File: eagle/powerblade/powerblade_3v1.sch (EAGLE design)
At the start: 93 parts, among them J1 JTAG_14PIN_IDC, J21 AC_INTBFILM, J4 TC2030-JLINK-NL, Q1 2N7002, Q3 2SK1829, Q4 2SK1829, U1 TPS62122, U2 MCP6V3, U3 MSP430FR5738, U4 NRF51822QF, U6 MAX9910, U7 OPA2369, X1 16MHz, X2 ABS05-32.768KHZ-9-T, X3 32.768kHz

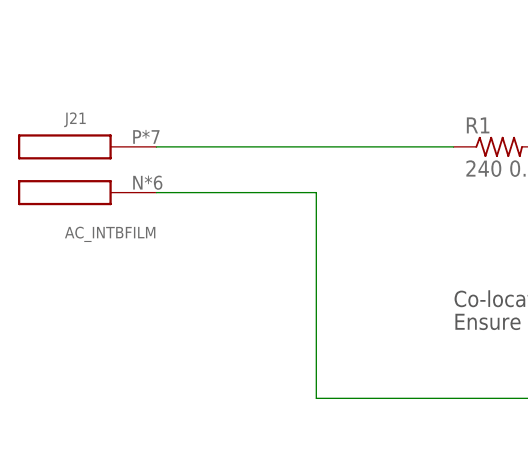
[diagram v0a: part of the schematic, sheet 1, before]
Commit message: updated phase and neutral and updated in powerblade
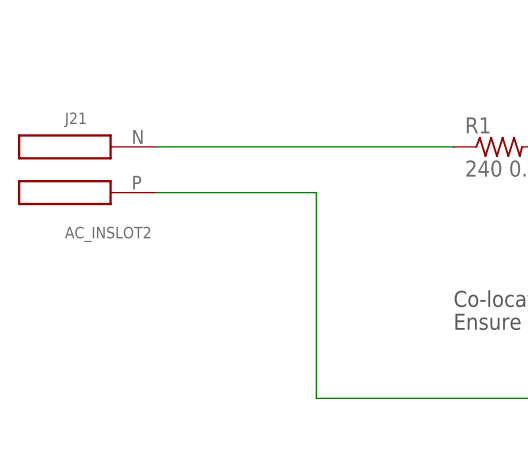
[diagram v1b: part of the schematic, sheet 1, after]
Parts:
- J21: value AC_INTBFILM -> AC_INSLOT2; device powerfilm:AC_INTBFILM -> powerfilm:AC_INSLOT2
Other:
- moved on the sheet: J21
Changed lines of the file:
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@@
 <part name="GND1" library="supply1" deviceset="GND" device=""/>
 <part name="P+1" library="supply1" deviceset="VCC" device=""/>
-<part name="J21" library="powerfilm" deviceset="AC_IN" device="TBFILM" value="AC_INTBFILM">
+<part name="J21" library="powerfilm" deviceset="AC_IN" device="SLOT2" value="AC_INSLOT2">
 <attribute name="DIGIKEY" value="NP"/>
 </part>

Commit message: updates to powerblade board
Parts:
- removed C1: 0.033uF 250VAC, rcl:C-EUC2220K
- removed R1: 240 0.25W, rcl:R-US_R0603
- removed R8: 1M, rcl:R-US_R0603
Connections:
- removed net N$12: J21.P, R1.1
- net N$2: no longer C1.1, R8.2
- net VTEST: now also J21.P; no longer C1.2, R1.2, R8.1
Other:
- moved on the sheet: R3

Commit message: placement work for powerblade 3v1
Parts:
- added C1: 33uF, rcl:CPOL-US0805_SM
- C10, C3, C7: device rcl:C-EUC0603 -> rcl:C-EUC0603_SM
- C28, C4, C8, C9: device rcl:C-EUC0402 -> rcl:C-EUC0402_SM
- C5: device rcl:C-EUC0603 -> rcl:C-EUC0805_SM
- R20, R21, R7, R9, RF, RI1, RI2: device rcl:R-US_R0402 -> rcl:R-US_R0402_SM
- R24: device rcl:R-US_R0603 -> rcl:R-US_R0603_SM
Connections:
- net +3V3: now also C5.1
- net GND: now also C1.-
- net VCC: now also C1.+; no longer C5.1

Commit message: changed v_sense amplifier to TI part
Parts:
- U6: DIGIKEY (none) -> 296-25252-1-ND
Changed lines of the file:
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@@
 <?xml version="1.0" encoding="utf-8"?>
 <!DOCTYPE eagle SYSTEM "eagle.dtd">
-<eagle version="6.3">
+<eagle version="6.5.0">
 <drawing>
 <settings>
@@
 <grid distance="0.1" unitdist="inch" unit="inch" style="lines" multiple="1" display="no" altdistance="0.01" altunitdist="inch" altunit="inch"/>
 <layers>
-<layer number="1" name="Top" color="4" fill="1" visible="yes" active="no"/>
-<layer number="2" name="Route2" color="1" fill="3" visible="yes" active="no"/>
-<layer number="3" name="Route3" color="4" fill="3" visible="yes" active="no"/>
-<layer number="4" name="Route4" color="1" fill="4" visible="yes" active="no"/>
-<layer number="5" name="Route5" color="4" fill="4" visible="yes" active="no"/>
-<layer number="6" name="Route6" color="1" fill="8" visible="yes" active="no"/>
-<layer number="7" name="Route7" color="4" fill="8" visible="yes" active="no"/>
-<layer number="8" name="Route8" color="1" fill="2" visible="yes" active="no"/>
-<layer number="9" name="Route9" color="4" fill="2" visible="yes" active="no"/>
-<layer number="10" name="Route10" color="1" fill="7" visible="yes" active="no"/>
-<layer number="11" name="Route11" color="4" fill="7" visible="yes" active="no"/>
-<layer number="12" name="Route12" color="1" fill="5" visible="yes" active="no"/>
-<layer number="13" name="Route13" color="4" fill="5" visible="yes" active="no"/>
-<layer number="14" name="Route14" color="1" fill="6" visible="yes" active="no"/>
-<layer number="15" name="Route15" color="4" fill="6" visible="yes" active="no"/>
-<layer number="16" name="Bottom" color="1" fill="1" visible="yes" active="no"/>
-<layer number="17" name="Pads" color="2" fill="1" visible="yes" active="no"/>
-<layer number="18" name="Vias" color="2" fill="1" visible="yes" active="no"/>
-<layer number="19" name="Unrouted" color="6" fill="1" visible="yes" active="no"/>
-<layer number="20" name="Dimension" color="15" fill="1" visible="yes" active="no"/>
-<layer number="21" name="tPlace" color="7" fill="1" visible="yes" active="no"/>
-<layer number="22" name="bPlace" color="7" fill="1" visible="yes" active="no"/>
-<layer number="23" name="tOrigins" color="15" fill="1" visible="yes" active="no"/>
-<layer number="24" name="bOrigins" color="15" fill="1" visible="yes" active="no"/>
-<layer number="25" name="tNames" color="7" fill="1" visible="yes" active="no"/>
-<layer number="26" name="bNames" color="7" fill="1" visible="yes" active="no"/>
-<layer number="27" name="tValues" color="7" fill="1" visible="yes" active="no"/>
-<layer number="28" name="bValues" color="7" fill="1" visible="yes" active="no"/>
+<layer number="1" name="Top" color="4" fill="1" visible="no" active="no"/>
+<layer number="2" name="Route2" color="1" fill="3" visible="no" active="no"/>
+<layer number="3" name="Route3" color="4" fill="3" visible="no" active="no"/>
+<layer number="4" name="Route4" color="1" fill="4" visible="no" active="no"/>
+<layer number="5" name="Route5" color="4" fill="4" visible="no" active="no"/>
+<layer number="6" name="Route6" color="1" fill="8" visible="no" active="no"/>
+<layer number="7" name="Route7" color="4" fill="8" visible="no" active="no"/>
+<layer number="8" name="Route8" color="1" fill="2" visible="no" active="no"/>
+<layer number="9" name="Route9" color="4" fill="2" visible="no" active="no"/>
+<layer number="10" name="Route10" color="1" fill="7" visible="no" active="no"/>
+<layer number="11" name="Route11" color="4" fill="7" visible="no" active="no"/>
+<layer number="12" name="Route12" color="1" fill="5" visible="no" active="no"/>
+<layer number="13" name="Route13" color="4" fill="5" visible="no" active="no"/>
+<layer number="14" name="Route14" color="1" fill="6" visible="no" active="no"/>
+<layer number="15" name="Route15" color="4" fill="6" visible="no" active="no"/>
+<layer number="16" name="Bottom" color="1" fill="1" visible="no" active="no"/>
+<layer number="17" name="Pads" color="2" fill="1" visible="no" active="no"/>
+<layer number="18" name="Vias" color="2" fill="1" visible="no" active="no"/>
+<layer number="19" name="Unrouted" color="6" fill="1" visible="no" active="no"/>
+<layer number="20" name="Dimension" color="15" fill="1" visible="no" active="no"/>
+<layer number="21" name="tPlace" color="7" fill="1" visible="no" active="no"/>
+<layer number="22" name="bPlace" color="7" fill="1" visible="no" active="no"/>
+<layer number="23" name="tOrigins" color="15" fill="1" visible="no" active="no"/>
+<layer number="24" name="bOrigins" color="15" fill="1" visible="no" active="no"/>
+<layer number="25" name="tNames" color="7" fill="1" visible="no" active="no"/>
+<layer number="26" name="bNames" color="7" fill="1" visible="no" active="no"/>
+<layer number="27" name="tValues" color="7" fill="1" visible="no" active="no"/>
+<layer number="28" name="bValues" color="7" fill="1" visible="no" active="no"/>
 <layer number="29" name="tStop" color="7" fill="3" visible="no" active="no"/>
 <layer number="30" name="bStop" color="7" fill="6" visible="no" active="no"/>
@@
 <layer number="35" name="tGlue" color="7" fill="4" visible="no" active="no"/>
 <layer number="36" name="bGlue" color="7" fill="5" visible="no" active="no"/>
-<layer number="37" name="tTest" color="7" fill="1" visible="yes" active="no"/>
-<layer number="38" name="bTest" color="7" fill="1" visible="yes" active="no"/>
+<layer number="37" name="tTest" color="7" fill="1" visible="no" active="no"/>
+<layer number="38" name="bTest" color="7" fill="1" visible="no" active="no"/>
 <layer number="39" name="tKeepout" color="4" fill="11" visible="no" active="no"/>
 <layer number="40" name="bKeepout" color="1" fill="11" visible="no" active="no"/>
@@
 <layer number="44" name="Drills" color="7" fill="1" visible="no" active="no"/>
 <layer number="45" name="Holes" color="7" fill="1" visible="no" active="no"/>
-<layer number="46" name="Milling" color="3" fill="1" visible="yes" active="no"/>
-<layer number="47" name="Measures" color="7" fill="1" visible="yes" active="no"/>
-<layer number="48" name="Document" color="7" fill="1" visible="yes" active="no"/>
-<layer number="49" name="Reference" color="7" fill="1" visible="yes" active="no"/>
-<layer number="50" name="dxf" color="7" fill="1" visible="yes" active="no"/>
-<layer number="51" name="tDocu" color="7" fill="1" visible="yes" active="no"/>
-<layer number="52" name="bDocu" color="7" fill="1" visible="yes" active="no"/>
-<layer number="53" name="tGND_GNDA" color="7" fill="9" visible="yes" active="no"/>
-<layer number="54" name="bGND_GNDA" color="1" fill="9" visible="yes" active="no"/>
-<layer number="56" name="wert" color="7" fill="1" visible="yes" active="no"/>
-<layer number="57" name="tCAD" color="7" fill="1" visible="yes" active="no"/>
+<layer number="46" name="Milling" color="3" fill="1" visible="no" active="no"/>
+<layer number="47" name="Measures" color="7" fill="1" visible="no" active="no"/>
+<layer number="48" name="Document" color="7" fill="1" visible="no" active="no"/>
+<layer number="49" name="Reference" color="7" fill="1" visible="no" active="no"/>
+<layer number="50" name="dxf" color="7" fill="1" visible="no" active="no"/>
+<layer number="51" name="tDocu" color="7" fill="1" visible="no" active="no"/>
+<layer number="52" name="bDocu" color="7" fill="1" visible="no" active="no"/>
+<layer number="53" name="tGND_GNDA" color="7" fill="9" visible="no" active="no"/>
+<layer number="54" name="bGND_GNDA" color="1" fill="9" visible="no" active="no"/>
+<layer number="56" name="wert" color="7" fill="1" visible="no" active="no"/>
+<layer number="57" name="tCAD" color="7" fill="1" visible="no" active="no"/>
 <layer number="91" name="Nets" color="2" fill="1" visible="yes" active="yes"/>
 <layer number="92" name="Busses" color="1" fill="1" visible="yes" active="yes"/>
@@
 <attribute name="DIGIKEY" value="445-1265-1-ND"/>
 </part>
-<part name="U6" library="powerfilm" deviceset="MAX9910" device=""/>
+<part name="U6" library="powerfilm" deviceset="MAX9910" device="">
+<attribute name="DIGIKEY" value="296-25252-1-ND"/>
+</part>
 <part name="C28" library="rcl" deviceset="C-EU" device="C0402_SM" value="0.1uF">
 <attribute name="DIGIKEY" value="445-1265-1-ND"/>

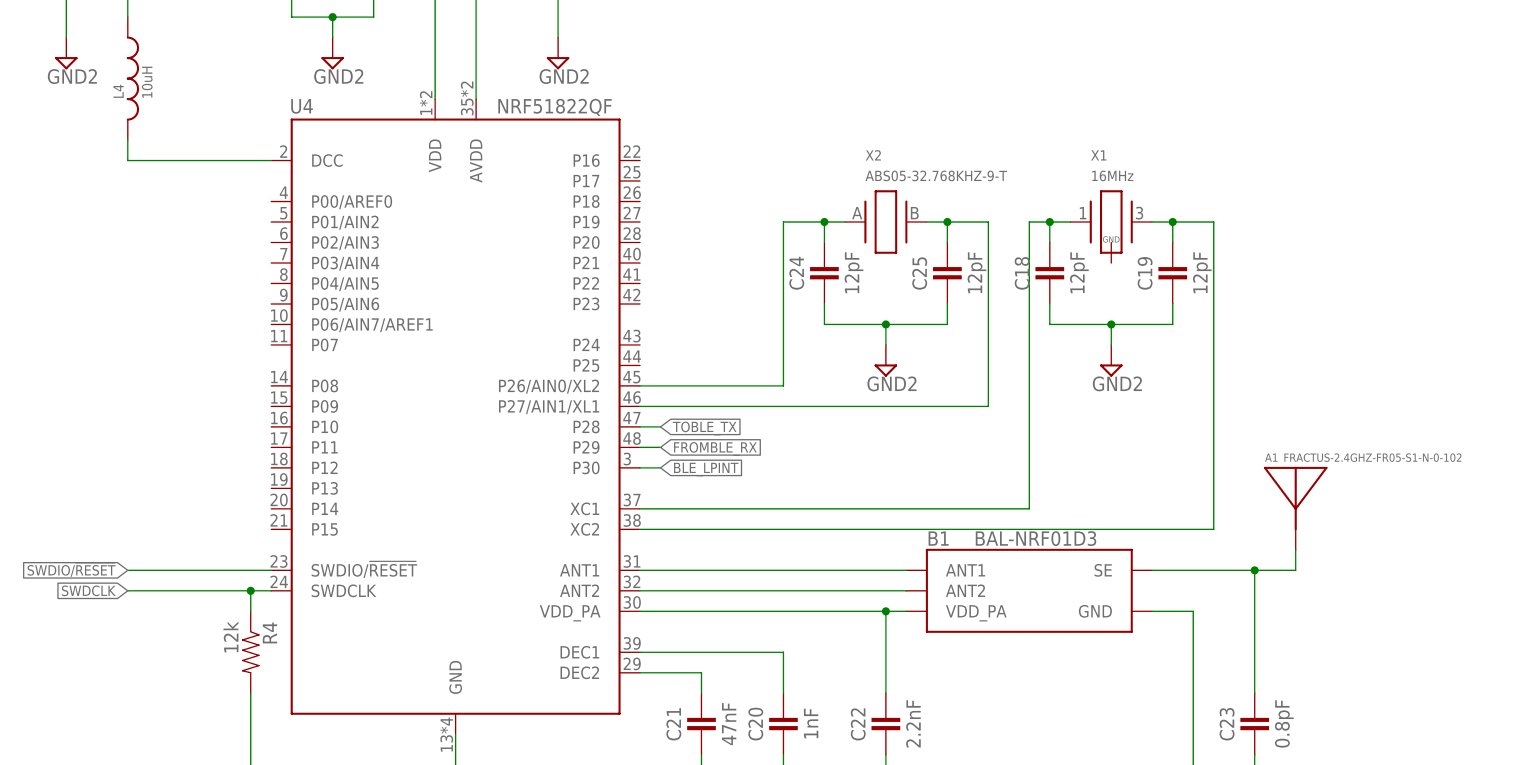
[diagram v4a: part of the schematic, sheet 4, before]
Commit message: placement for 51822 and 0402_sm for all passives in current sense
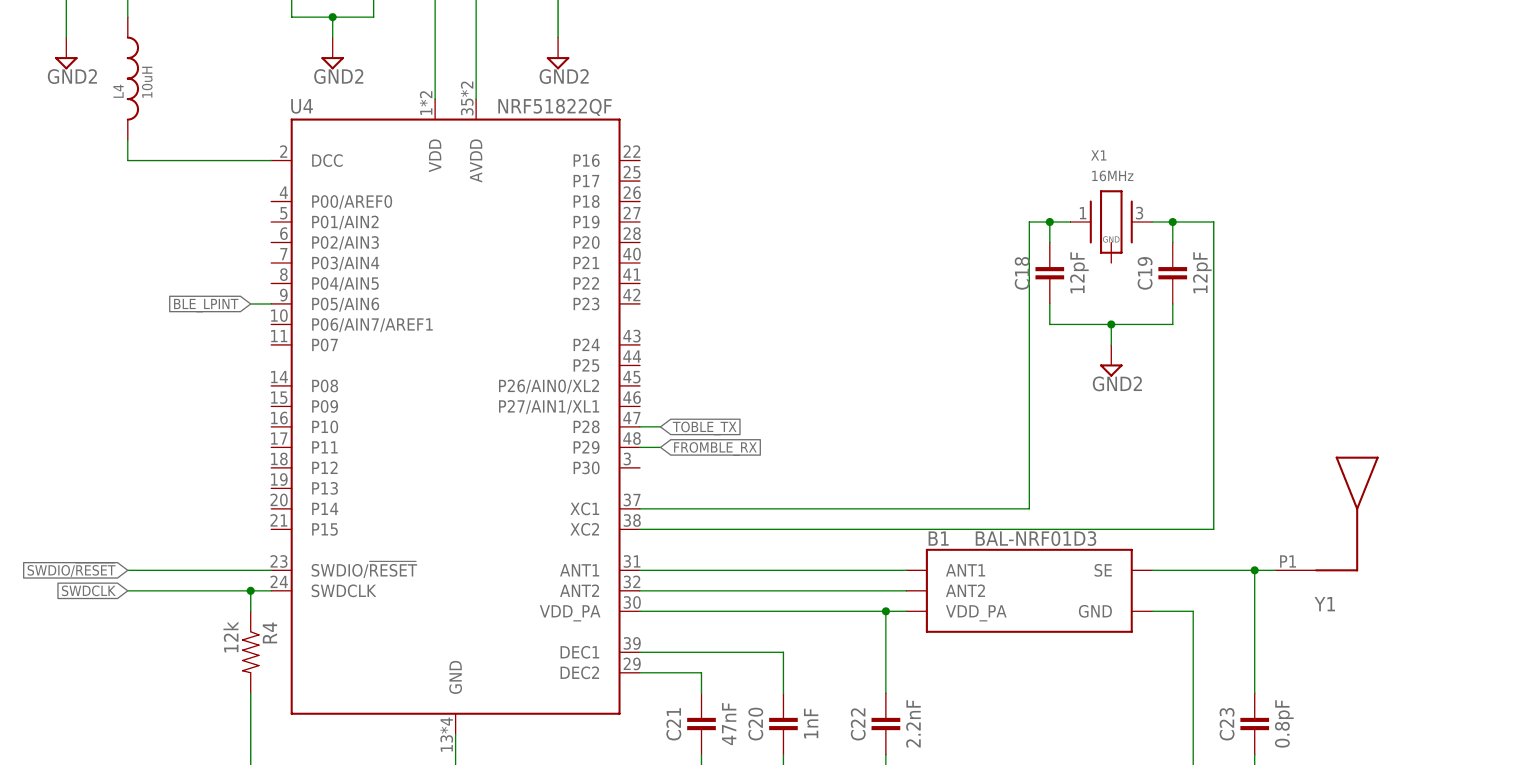
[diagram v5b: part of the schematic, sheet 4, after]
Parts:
- removed A1: FRACTUS-2.4GHZ-FR05-S1-N-0-102, chips:FRACTUS-2.4GHZ-FR05-S1-N-0-102
- removed C24, C25: 12pF, passives:CAPACITOR
- removed X2: ABS05-32.768KHZ-9-T, crystals:ABS05-32.768KHZ-9-T
- added R1: NP, rcl:R-US_R0402_SM
- added Y1: UREACH_XTEND, powerfilm:UREACH_XTEND
- C2: device rcl:C-EUC0603 -> rcl:C-EUC0402_SM
- C27, C38, C39: device rcl:C-EUC0402 -> rcl:C-EUC0402_SM
- R14, R15, R16, R17, R18, R35, R37, R38, R39, R40: device rcl:R-US_R0402 -> rcl:R-US_R0402_SM
- R2, R5: device rcl:R-US_R0603 -> rcl:R-US_R0402_SM
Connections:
- removed net A0: C24.1, U4.P26/AIN0/XL2, X2.1
- removed net A1: C25.1, U4.P27/AIN1/XL1, X2.2
- net BLE_LPINT: now also U4.P05/AIN6; no longer U4.P30
- net GND2: no longer C24.2, C25.2
- net N$37: now also R1.1
- net N$4: now also Y1.P1; no longer A1.ANTENNA
- net N$65: now also R1.2

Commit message: finished placement
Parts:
- C14: device rcl:C-EUC0603 -> rcl:C-EUC0402_SM; DIGIKEY 445-1316-1-ND -> (none)
- C15: device rcl:C-EUC0603 -> rcl:C-EUC0603_SM; DIGIKEY 1276-1119-1-ND -> (none)
- C16, C34, C6: device rcl:C-EUC0603 -> rcl:C-EUC0402_SM
- R10, R11, R12, R13, R22: device rcl:R-US_R0603 -> rcl:R-US_R0402_SM
- R19: device rcl:R-US_R0603 -> rcl:R-US_R0402_SM; DIGIKEY P47KGCT-ND -> (none)
- R6: device rcl:R-US_R0603 -> rcl:R-US_R0603_SM
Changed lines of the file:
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@@
 </part>
 <part name="U3" library="powerfilm" deviceset="MSP430FR5738" device=""/>
-<part name="C14" library="rcl" deviceset="C-EU" device="C0603" value="0.1uF">
-<attribute name="DIGIKEY" value="445-1316-1-ND"/>
-</part>
-<part name="C15" library="rcl" deviceset="C-EU" device="C0603" value="10uF">
-<attribute name="DIGIKEY" value="1276-1119-1-ND"/>
-</part>
-<part name="C16" library="rcl" deviceset="C-EU" device="C0603" value="470nF">
+<part name="C14" library="rcl" deviceset="C-EU" device="C0402_SM" value="0.1uF"/>
+<part name="C15" library="rcl" deviceset="C-EU" device="C0603_SM" value="10uF"/>
+<part name="C16" library="rcl" deviceset="C-EU" device="C0402_SM" value="470nF">
 <attribute name="DIGIKEY" value="445-5192-1-ND"/>
 </part>
@@
 <part name="GND21" library="supply1" deviceset="GND" device=""/>
 <part name="+3V4" library="supply1" deviceset="+3V3" device=""/>
-<part name="R19" library="rcl" deviceset="R-US_" device="R0603" value="47k">
-<attribute name="DIGIKEY" value="P47KGCT-ND"/>
-</part>
+<part name="R19" library="rcl" deviceset="R-US_" device="R0402_SM" value="47k"/>
 <part name="GND22" library="supply1" deviceset="GND" device=""/>
 <part name="J1" library="ibat" deviceset="JTAG_14PIN" device="_IDC" value="JTAG_14PIN_IDC">
@@
 <part name="+3V7" library="supply1" deviceset="+3V3" device=""/>
 <part name="GND23" library="supply1" deviceset="GND" device=""/>
-<part name="R11" library="rcl" deviceset="R-US_" device="R0603" value="670k"/>
-<part name="R12" library="rcl" deviceset="R-US_" device="R0603" value="330k"/>
+<part name="R11" library="rcl" deviceset="R-US_" device="R0402_SM" value="670k"/>
+<part name="R12" library="rcl" deviceset="R-US_" device="R0402_SM" value="330k"/>
 <part name="GND25" library="supply1" deviceset="GND" device=""/>
 <part name="P+4" library="supply1" deviceset="VCC" device=""/>
@@
 <attribute name="DIGIKEY" value="535-12373-1-ND"/>
 </part>
-<part name="C6" library="rcl" deviceset="C-EU" device="C0603" value="8pF">
+<part name="C6" library="rcl" deviceset="C-EU" device="C0402_SM" value="8pF">
 <attribute name="DIGIKEY" value="1276-1817-1-ND"/>
 </part>
-<part name="C34" library="rcl" deviceset="C-EU" device="C0603" value="8pF">
+<part name="C34" library="rcl" deviceset="C-EU" device="C0402_SM" value="8pF">
 <attribute name="DIGIKEY" value="1276-1817-1-ND"/>
 </part>
@@
 <part name="Q4" library="powerfilm" deviceset="2SK1829" device=""/>
 <part name="SUPPLY19" library="supply2" deviceset="GND3" device=""/>
-<part name="R6" library="rcl" deviceset="R-US_" device="R0603" value="660k"/>
+<part name="R6" library="rcl" deviceset="R-US_" device="R0603_SM" value="660k"/>
 <part name="SUPPLY20" library="supply2" deviceset="GND3" device=""/>
 <part name="SUPPLY21" library="supply2" deviceset="GND3" device=""/>
@@
 <part name="SUPPLY28" library="supply2" deviceset="GND3" device=""/>
 <part name="GND2" library="supply1" deviceset="GND" device=""/>
-<part name="R10" library="rcl" deviceset="R-US_" device="R0603" value="220k"/>
-<part name="R13" library="rcl" deviceset="R-US_" device="R0603" value="330k"/>
-<part name="R22" library="rcl" deviceset="R-US_" device="R0603" value="670k"/>
+<part name="R10" library="rcl" deviceset="R-US_" device="R0402_SM" value="220k"/>
+<part name="R13" library="rcl" deviceset="R-US_" device="R0402_SM" value="330k"/>
+<part name="R22" library="rcl" deviceset="R-US_" device="R0402_SM" value="670k"/>
 <part name="GND8" library="supply1" deviceset="GND" device=""/>
 <part name="R24" library="rcl" deviceset="R-US_" device="R0603_SM" value="1 1%">
@@
 <instances>
 <instance part="U3" gate="G$1" x="0" y="0"/>
-<instance part="C14" gate="G$1" x="-35.56" y="35.56">
-<attribute name="DIGIKEY" x="-35.56" y="35.56" size="1.27" layer="96" display="off"/>
-</instance>
-<instance part="C15" gate="G$1" x="-45.72" y="35.56">
-<attribute name="DIGIKEY" x="-45.72" y="35.56" size="1.27" layer="96" display="off"/>
-</instance>
+<instance part="C14" gate="G$1" x="-35.56" y="35.56"/>
+<instance part="C15" gate="G$1" x="-45.72" y="35.56"/>
 <instance part="C16" gate="G$1" x="-43.18" y="15.24" smashed="yes" rot="R90">
 <attribute name="NAME" x="-41.656" y="18.161" size="1.778" layer="95"/>
@@
 <instance part="GND21" gate="1" x="-48.26" y="10.16"/>
 <instance part="+3V4" gate="G$1" x="-35.56" y="50.8"/>
-<instance part="R19" gate="G$1" x="-55.88" y="33.02" rot="R90">
-<attribute name="DIGIKEY" x="-55.88" y="33.02" size="1.27" layer="96" rot="R90" display="off"/>
-</instance>
+<instance part="R19" gate="G$1" x="-55.88" y="33.02" rot="R90"/>
 <instance part="GND22" gate="1" x="27.94" y="-27.94"/>
 <instance part="J1" gate="G$1" x="17.78" y="48.26">

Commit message: updates and routing in powerblade
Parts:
- removed C13: 4.7uF, passives:CAPACITOR
- added C24: 0.1uF, rcl:C-EUC0402_SM
- added TP4, TP5, TP6, TP7, TP8: TP_LONG, skyspecs:TP_LONG
- C11: value 0.1uF -> 4.7uF; device passives:CAPACITOR -> rcl:C-EUC0402_SM; DIGIKEY 445-4952-1-ND -> 445-5947-1-ND
- J1: value JTAG_14PIN_IDC -> JTAG_14PIN_IDC-NL; device ibat:JTAG_14PIN_IDC -> ibat:JTAG_14PIN_IDC-NL
- R23: device rcl:R-US_R0603 -> rcl:R-US_R0603_SM
- renumbered RS+ to TP10, RS- to TP9, VS+ to TP12, VS- to TP11
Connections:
- removed net N$8: R13.2, R22.1, U3.P1.0/VREF-
- new net ZC_LOW: R13.2, R22.1, TP8.P$1, U3.P1.0/VREF-
- net +3V3: now also C24.1; no longer C13.1
- net BLE_LPINT: now also U4.P08; no longer U4.P05/AIN6
- net FROMBLE_RX: now also TP7.P$1
- net GND2: now also C24.2; no longer C13.2
- net PWM_CURRENT: now also TP4.P$1
- net PWM_VOLTAGE: now also TP5.P$1
- net TOBLE_TX: now also TP6.P$1
